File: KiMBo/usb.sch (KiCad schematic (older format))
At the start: 19 parts, among them U10 74LVC2G241, U11 TPD4S012, U2 OSD3358, U8 TPS2051B, U9 TPD4S012

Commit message: Replace most electrolytic cap symbols symbols with the standard, non-polarized (ceramic) cap symbol
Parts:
- C27, C28, C29: symbol CP1 -> C
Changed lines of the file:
@@
 $EndComp
 $Comp
-L CP1 C29
+L C C29
 U 1 1 584F50A3
 P 8150 1650
@@
 $EndComp
 $Comp
-L CP1 C27
+L C C27
 U 1 1 58524285
 P 6250 4600
@@
 $EndComp
 $Comp
-L CP1 C26
-U 1 1 5852A62D
-P 2500 4400
-F 0 "C26" H 2615 4446 50  0000 L CNN
-F 1 "220μF" H 2615 4355 50  0000 L CNN
-F 2 "" H 2500 4400 50  0001 C CNN
-F 3 "" H 2500 4400 50  0000 C CNN
-	1    2500 4400
-	-1   0    0    -1
-$EndComp
-$Comp
 L GND #PWR0115
 U 1 1 5852A6BE
@@
 $EndComp
 $Comp
-L CP1 C28
+L C C28
 U 1 1 5852C2E6
 P 8000 4100
@@
 	6550 2050 6550 1600
 Wire Wire Line
-	6550 1600 7700 1600
+	6550 1600 7600 1600
+Wire Wire Line
+	7600 1600 7700 1600
 Wire Wire Line
 	7600 1600 7600 2250
@@
 	3600 1600 3600 1650
 Wire Wire Line
-	3450 1650 3650 1650
-Wire Wire Line
-	3450 1750 3650 1750
+	3450 1650 3600 1650
+Wire Wire Line
+	3600 1650 3650 1650
+Wire Wire Line
+	3450 1750 3500 1750
+Wire Wire Line
+	3500 1750 3650 1750
 Wire Wire Line
 	3600 1250 3600 1300
@@
 	3500 1300 3500 1250
 Wire Wire Line
-	3500 1250 3600 1250
+	3500 1250 3550 1250
+Wire Wire Line
+	3550 1250 3600 1250
 Wire Wire Line
 	3550 1200 3550 1250
@@
 	5150 4200 6400 4200
 Wire Wire Line
-	4450 4100 5850 4100
+	4450 4100 4500 4100
+Wire Wire Line
+	4500 4100 5750 4100
+Wire Wire Line
+	5750 4100 5850 4100
 Wire Wire Line
 	6100 4800 6250 4800
 Wire Wire Line
-	6250 4750 6250 4850
+	6250 4750 6250 4800
+Wire Wire Line
+	6250 4800 6250 4850
 Connection ~ 6250 4800
 Wire Wire Line
 	6100 4600 6100 4400
 Wire Wire Line
-	5750 4400 6250 4400
+	5750 4400 6100 4400
+Wire Wire Line
+	6100 4400 6250 4400
 Wire Wire Line
 	6250 4400 6250 4450
@@
 	5150 4700 5150 4200
 Wire Wire Line
-	5750 4050 5750 4400
+	5750 4050 5750 4100
+Wire Wire Line
+	5750 4100 5750 4400
 Connection ~ 6100 4400
 Connection ~ 5750 4100
@@
 	4500 4300 4450 4300
 Wire Wire Line
-	4500 4100 4500 4300
+	4500 4100 4500 4200
+Wire Wire Line
+	4500 4200 4500 4300
 Wire Wire Line
 	4450 4200 4500 4200
@@
 	4500 4500 4450 4500
 Wire Wire Line
-	4450 4400 4700 4400
+	4450 4400 4550 4400
+Wire Wire Line
+	4550 4400 4700 4400
 Wire Wire Line
 	5050 4350 5050 4400
@@
 Connection ~ 4550 4400
 Wire Wire Line
-	2500 4200 3550 4200
+	2500 4200 3500 4200
+Wire Wire Line
+	3500 4200 3550 4200
 Wire Wire Line
 	3500 4200 3500 4300
@@
 	3500 4300 3550 4300
 Wire Wire Line
-	2500 4150 2500 4250
+	2500 4150 2500 4200
+Wire Wire Line
+	2500 4200 2500 4250
 Connection ~ 3500 4200
 Wire Wire Line
@@
 	2700 4100 2700 4250
 Wire Wire Line
-	2800 4400 3550 4400
+	2800 4400 3500 4400
+Wire Wire Line
+	3500 4400 3550 4400
 Wire Wire Line
 	3500 4450 3500 4400
@@
 	8150 4300 8000 4300
 Wire Wire Line
-	8000 4250 8000 4350
-Wire Wire Line
-	8150 3850 8150 4100
+	8000 4250 8000 4300
+Wire Wire Line
+	8000 4300 8000 4350
+Wire Wire Line
+	8150 3850 8150 3900
+Wire Wire Line
+	8150 3900 8150 4100
 Wire Wire Line
 	8150 3900 8000 3900
@@
 F 0 "R53" H 5819 3946 50  0000 L CNN
 F 1 "100mΩ" H 5819 3855 50  0000 L CNN
-F 2 "" V 5680 3900 50  0000 C CNN
+F 2 "" V 5680 3900 50  0001 C CNN
 F 3 "" H 5750 3900 50  0000 C CNN
 	1    5750 3900
@@
 Text Notes 5200 3800 0    60   ~ 0
 73L3R10J
+$Comp
+L CP1 C26
+U 1 1 58EB0DF2
+P 2500 4400
+F 0 "C26" H 2615 4446 50  0000 L CNN
+F 1 "220μF" H 2615 4355 50  0000 L CNN
+F 2 "" H 2500 4400 50  0000 C CNN
+F 3 "" H 2500 4400 50  0000 C CNN
+	1    2500 4400
+	-1   0    0    -1
+$EndComp
 $EndSCHEMATC

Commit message: Associate more footprints
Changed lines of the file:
@@
 	6550 2050 6550 1600
 Wire Wire Line
-	6550 1600 7600 1600
-Wire Wire Line
-	7600 1600 7700 1600
+	6550 1600 7700 1600
 Wire Wire Line
 	7600 1600 7600 2250
@@
 	3600 1600 3600 1650
 Wire Wire Line
-	3450 1650 3600 1650
-Wire Wire Line
-	3600 1650 3650 1650
-Wire Wire Line
-	3450 1750 3500 1750
-Wire Wire Line
-	3500 1750 3650 1750
+	3450 1650 3650 1650
+Wire Wire Line
+	3450 1750 3650 1750
 Wire Wire Line
 	3600 1250 3600 1300
@@
 	3500 1300 3500 1250
 Wire Wire Line
-	3500 1250 3550 1250
-Wire Wire Line
-	3550 1250 3600 1250
+	3500 1250 3600 1250
 Wire Wire Line
 	3550 1200 3550 1250
@@
 	5150 4200 6400 4200
 Wire Wire Line
-	4450 4100 4500 4100
-Wire Wire Line
-	4500 4100 5750 4100
-Wire Wire Line
-	5750 4100 5850 4100
+	4450 4100 5850 4100
 Wire Wire Line
 	6100 4800 6250 4800
 Wire Wire Line
-	6250 4750 6250 4800
-Wire Wire Line
-	6250 4800 6250 4850
+	6250 4750 6250 4850
 Connection ~ 6250 4800
 Wire Wire Line
 	6100 4600 6100 4400
 Wire Wire Line
-	5750 4400 6100 4400
-Wire Wire Line
-	6100 4400 6250 4400
+	5750 4400 6250 4400
 Wire Wire Line
 	6250 4400 6250 4450
@@
 	5150 4700 5150 4200
 Wire Wire Line
-	5750 4050 5750 4100
-Wire Wire Line
-	5750 4100 5750 4400
+	5750 4050 5750 4400
 Connection ~ 6100 4400
 Connection ~ 5750 4100
@@
 	4500 4300 4450 4300
 Wire Wire Line
-	4500 4100 4500 4200
-Wire Wire Line
-	4500 4200 4500 4300
+	4500 4100 4500 4300
 Wire Wire Line
 	4450 4200 4500 4200
@@
 	4500 4500 4450 4500
 Wire Wire Line
-	4450 4400 4550 4400
-Wire Wire Line
-	4550 4400 4700 4400
+	4450 4400 4700 4400
 Wire Wire Line
 	5050 4350 5050 4400
@@
 Connection ~ 4550 4400
 Wire Wire Line
-	2500 4200 3500 4200
-Wire Wire Line
-	3500 4200 3550 4200
+	2500 4200 3550 4200
 Wire Wire Line
 	3500 4200 3500 4300
@@
 	3500 4300 3550 4300
 Wire Wire Line
-	2500 4150 2500 4200
-Wire Wire Line
-	2500 4200 2500 4250
+	2500 4150 2500 4250
 Connection ~ 3500 4200
 Wire Wire Line
@@
 	2700 4100 2700 4250
 Wire Wire Line
-	2800 4400 3500 4400
-Wire Wire Line
-	3500 4400 3550 4400
+	2800 4400 3550 4400
 Wire Wire Line
 	3500 4450 3500 4400
@@
 	8150 4300 8000 4300
 Wire Wire Line
-	8000 4250 8000 4300
-Wire Wire Line
-	8000 4300 8000 4350
-Wire Wire Line
-	8150 3850 8150 3900
-Wire Wire Line
-	8150 3900 8150 4100
+	8000 4250 8000 4350
+Wire Wire Line
+	8150 3850 8150 4100
 Wire Wire Line
 	8150 3900 8000 3900
@@
 F 0 "C26" H 2615 4446 50  0000 L CNN
 F 1 "220μF" H 2615 4355 50  0000 L CNN
-F 2 "" H 2500 4400 50  0000 C CNN
+F 2 "" H 2500 4400 50  0001 C CNN
 F 3 "" H 2500 4400 50  0000 C CNN
 	1    2500 4400

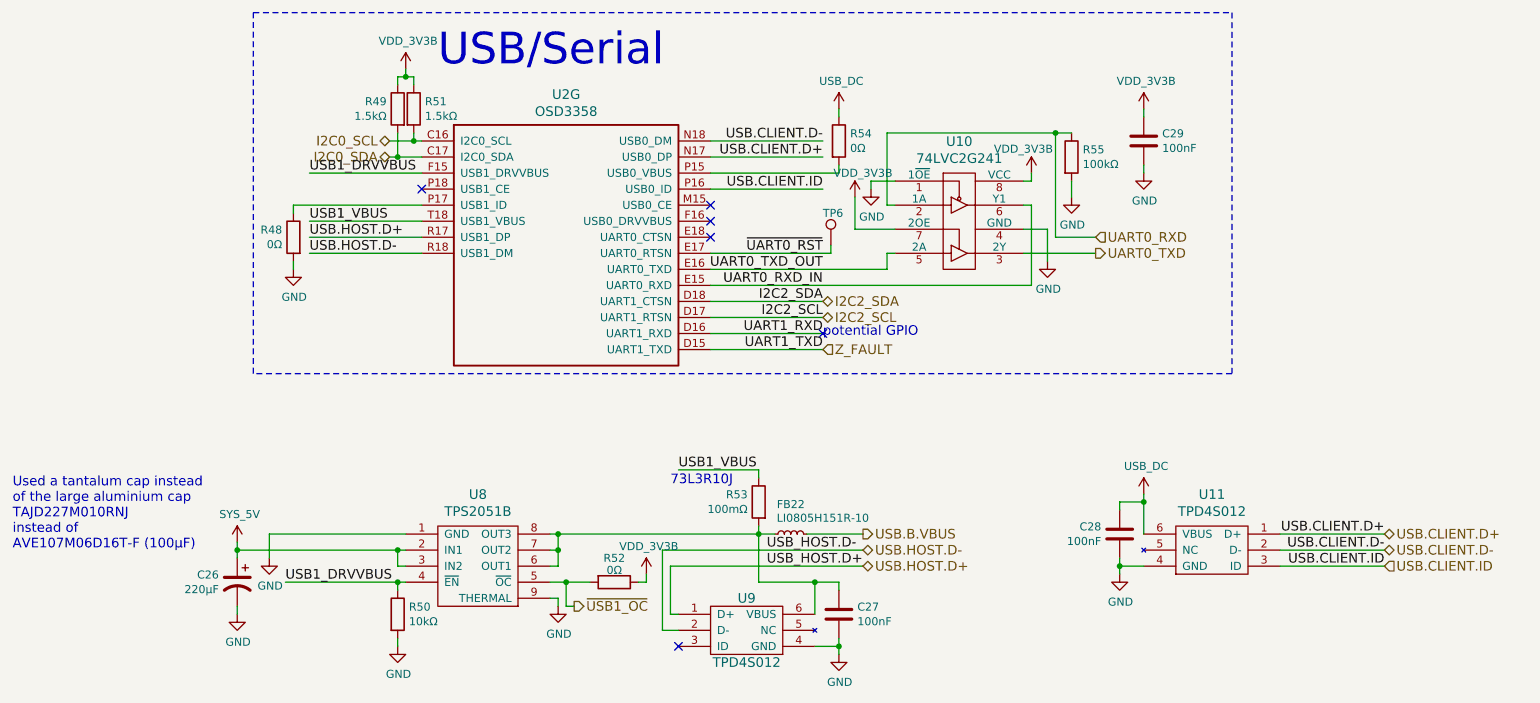
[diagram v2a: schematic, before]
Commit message: Add equivalent annotations document, associate more footprints
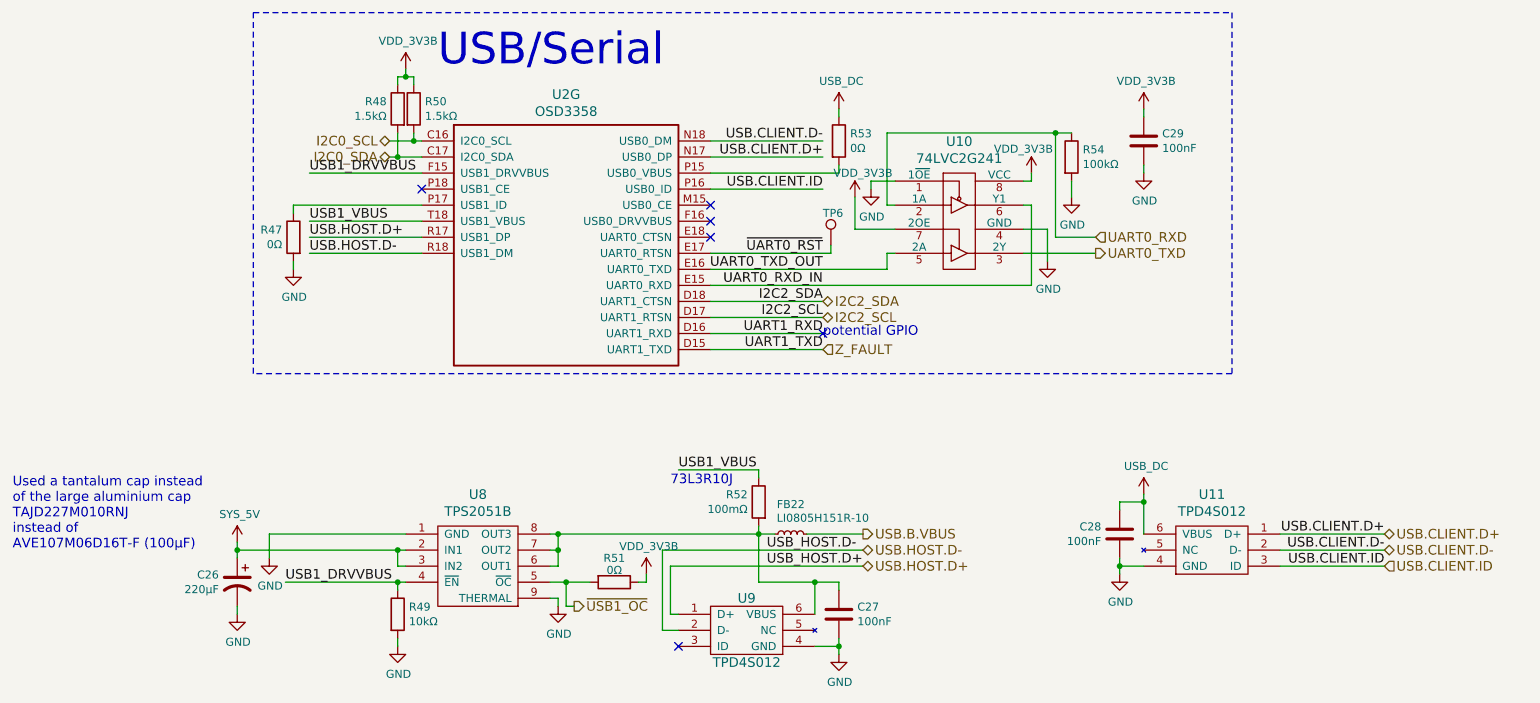
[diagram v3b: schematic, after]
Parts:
- C27, C28, C29: footprint (none) -> Capacitors_SMD:C_0402
- R47: renamed from R48; footprint (none) -> Resistors_SMD:R_0402
- R48: renamed from R49; footprint (none) -> Resistors_SMD:R_0402
- R49: renamed from R50; footprint (none) -> Resistors_SMD:R_0402
- R50: renamed from R51; footprint (none) -> Resistors_SMD:R_0402
- R51: renamed from R52; footprint (none) -> Resistors_SMD:R_0402
- R52: renamed from R53; footprint (none) -> Resistors_SMD:R_0402
- R53: renamed from R54; footprint (none) -> Resistors_SMD:R_0402
- R54: renamed from R55; footprint (none) -> Resistors_SMD:R_0402
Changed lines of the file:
@@
 $EndComp
 $Comp
-L GND #PWR0108
+L GND #PWR0107
 U 1 1 584F5078
 P 7550 2400
-F 0 "#PWR0108" H 7550 2150 50  0001 C CNN
+F 0 "#PWR0107" H 7550 2150 50  0001 C CNN
 F 1 "GND" H 7555 2227 50  0000 C CNN
 F 2 "" H 7550 2400 50  0000 C CNN
@@
 UART0_RXD_IN
 $Comp
-L R R55
+L R R54
 U 1 1 584F5085
 P 7700 1750
-F 0 "R55" H 7770 1796 50  0000 L CNN
+F 0 "R54" H 7770 1796 50  0000 L CNN
 F 1 "100kΩ" H 7770 1705 50  0000 L CNN
-F 2 "" V 7630 1750 50  0001 C CNN
+F 2 "Resistors_SMD:R_0402" V 7630 1750 50  0001 C CNN
 F 3 "" H 7700 1750 50  0000 C CNN
 	1    7700 1750
@@
 $EndComp
 $Comp
-L GND #PWR0109
+L GND #PWR0108
 U 1 1 584F508C
 P 6450 1950
-F 0 "#PWR0109" H 6450 1700 50  0001 C CNN
+F 0 "#PWR0108" H 6450 1700 50  0001 C CNN
 F 1 "GND" H 6455 1777 50  0000 C CNN
 F 2 "" H 6450 1950 50  0000 C CNN
@@
 UART0_TXD_OUT
 $Comp
-L GND #PWR0110
+L GND #PWR0109
 U 1 1 584F509A
 P 7700 2000
-F 0 "#PWR0110" H 7700 1750 50  0001 C CNN
+F 0 "#PWR0109" H 7700 1750 50  0001 C CNN
 F 1 "GND" H 7705 1827 50  0000 C CNN
 F 2 "" H 7700 2000 50  0000 C CNN
@@
 F 0 "C29" H 8265 1696 50  0000 L CNN
 F 1 "100nF" H 8265 1605 50  0000 L CNN
-F 2 "" H 8150 1650 50  0001 C CNN
+F 2 "Capacitors_SMD:C_0402" H 8150 1650 50  0001 C CNN
 F 3 "" H 8150 1650 50  0000 C CNN
 	1    8150 1650
@@
 $EndComp
 $Comp
-L GND #PWR0111
+L GND #PWR0110
 U 1 1 584F50AA
 P 8150 1850
-F 0 "#PWR0111" H 8150 1600 50  0001 C CNN
+F 0 "#PWR0110" H 8150 1600 50  0001 C CNN
 F 1 "GND" H 8155 1677 50  0000 C CNN
 F 2 "" H 8150 1850 50  0000 C CNN
@@
 NoConn ~ 5450 2150
 $Comp
-L R R54
+L R R53
 U 1 1 584F50C1
 P 6250 1650
-F 0 "R54" H 6320 1696 50  0000 L CNN
+F 0 "R53" H 6320 1696 50  0000 L CNN
 F 1 "0Ω" H 6320 1605 50  0000 L CNN
-F 2 "" V 6180 1650 50  0001 C CNN
+F 2 "Resistors_SMD:R_0402" V 6180 1650 50  0001 C CNN
 F 3 "" H 6250 1650 50  0000 C CNN
 	1    6250 1650
@@
 NoConn ~ 3650 1950
 $Comp
-L R R48
+L R R47
 U 1 1 584F50D1
 P 2850 2250
-F 0 "R48" H 2920 2296 50  0000 L CNN
+F 0 "R47" H 2920 2296 50  0000 L CNN
 F 1 "0Ω" H 2920 2205 50  0000 L CNN
-F 2 "" V 2780 2250 50  0001 C CNN
+F 2 "Resistors_SMD:R_0402" V 2780 2250 50  0001 C CNN
 F 3 "" H 2850 2250 50  0000 C CNN
 	1    2850 2250
@@
 $EndComp
 $Comp
-L GND #PWR0112
+L GND #PWR0111
 U 1 1 584F50D8
 P 2850 2450
-F 0 "#PWR0112" H 2850 2200 50  0001 C CNN
+F 0 "#PWR0111" H 2850 2200 50  0001 C CNN
 F 1 "GND" H 2855 2277 50  0000 C CNN
 F 2 "" H 2850 2450 50  0000 C CNN
@@
 USB1_DRVVBUS
 $Comp
-L R R49
+L R R48
 U 1 1 584F50E0
 P 3500 1450
-F 0 "R49" H 3569 1496 50  0000 L CNN
+F 0 "R48" H 3569 1496 50  0000 L CNN
 F 1 "1.5kΩ" H 3569 1405 50  0000 L CNN
-F 2 "" V 3430 1450 50  0001 C CNN
+F 2 "Resistors_SMD:R_0402" V 3430 1450 50  0001 C CNN
 F 3 "" H 3500 1450 50  0000 C CNN
 	1    3500 1450
@@
 $EndComp
 $Comp
-L R R51
+L R R50
 U 1 1 584F50E7
 P 3600 1450
-F 0 "R51" H 3670 1496 50  0000 L CNN
+F 0 "R50" H 3670 1496 50  0000 L CNN
 F 1 "1.5kΩ" H 3670 1405 50  0000 L CNN
-F 2 "" V 3530 1450 50  0001 C CNN
+F 2 "Resistors_SMD:R_0402" V 3530 1450 50  0001 C CNN
 F 3 "" H 3600 1450 50  0000 C CNN
 	1    3600 1450
@@
 F 0 "C27" H 6365 4646 50  0000 L CNN
 F 1 "100nF" H 6365 4555 50  0000 L CNN
-F 2 "" H 6250 4600 50  0001 C CNN
+F 2 "Capacitors_SMD:C_0402" H 6250 4600 50  0001 C CNN
 F 3 "" H 6250 4600 50  0000 C CNN
 	1    6250 4600
@@
 $EndComp
 $Comp
-L GND #PWR0113
+L GND #PWR0112
 U 1 1 585243B8
 P 6250 4850
-F 0 "#PWR0113" H 6250 4600 50  0001 C CNN
+F 0 "#PWR0112" H 6250 4600 50  0001 C CNN
 F 1 "GND" H 6255 4677 50  0000 C CNN
 F 2 "" H 6250 4850 50  0000 C CNN
@@
 $EndComp
 $Comp
-L GND #PWR0114
+L GND #PWR0113
 U 1 1 58528602
 P 4500 4550
-F 0 "#PWR0114" H 4500 4300 50  0001 C CNN
+F 0 "#PWR0113" H 4500 4300 50  0001 C CNN
 F 1 "GND" H 4505 4377 50  0000 C CNN
 F 2 "" H 4500 4550 50  0000 C CNN
@@
 $EndComp
 $Comp
-L R R52
+L R R51
 U 1 1 58528C30
 P 4850 4400
-F 0 "R52" V 4700 4400 50  0000 C CNN
+F 0 "R51" V 4700 4400 50  0000 C CNN
 F 1 "0Ω" V 4775 4400 50  0000 C CNN
-F 2 "" V 4780 4400 50  0001 C CNN
+F 2 "Resistors_SMD:R_0402" V 4780 4400 50  0001 C CNN
 F 3 "" H 4850 4400 50  0000 C CNN
 	1    4850 4400
@@
 $EndComp
 $Comp
-L GND #PWR0115
+L GND #PWR0114
 U 1 1 5852A6BE
 P 2500 4600
-F 0 "#PWR0115" H 2500 4350 50  0001 C CNN
+F 0 "#PWR0114" H 2500 4350 50  0001 C CNN
 F 1 "GND" H 2505 4427 50  0000 C CNN
 F 2 "" H 2500 4600 50  0000 C CNN
@@
 $EndComp
 $Comp
-L GND #PWR0116
+L GND #PWR0115
 U 1 1 5852A82F
 P 2700 4250
-F 0 "#PWR0116" H 2700 4000 50  0001 C CNN
+F 0 "#PWR0115" H 2700 4000 50  0001 C CNN
 F 1 "GND" H 2705 4077 50  0000 C CNN
 F 2 "" H 2700 4250 50  0000 C CNN
@@
 USB1_DRVVBUS
 $Comp
-L R R50
+L R R49
 U 1 1 5852B51B
 P 3500 4600
-F 0 "R50" H 3570 4646 50  0000 L CNN
+F 0 "R49" H 3570 4646 50  0000 L CNN
 F 1 "10kΩ" H 3570 4555 50  0000 L CNN
-F 2 "" V 3430 4600 50  0001 C CNN
+F 2 "Resistors_SMD:R_0402" V 3430 4600 50  0001 C CNN
 F 3 "" H 3500 4600 50  0000 C CNN
 	1    3500 4600
@@
 $EndComp
 $Comp
-L GND #PWR0117
+L GND #PWR0116
 U 1 1 5852B68C
 P 3500 4800
-F 0 "#PWR0117" H 3500 4550 50  0001 C CNN
+F 0 "#PWR0116" H 3500 4550 50  0001 C CNN
 F 1 "GND" H 3505 4627 50  0000 C CNN
 F 2 "" H 3500 4800 50  0000 C CNN
@@
 F 0 "C28" H 8115 4146 50  0000 L CNN
 F 1 "100nF" H 8115 4055 50  0000 L CNN
-F 2 "" H 8000 4100 50  0001 C CNN
+F 2 "Capacitors_SMD:C_0402" H 8000 4100 50  0001 C CNN
 F 3 "" H 8000 4100 50  0000 C CNN
 	1    8000 4100
@@
 I2C2_SDA
 $Comp
-L USB_DC #PWR0118
+L USB_DC #PWR0117
 U 1 1 59F94F9A
 P 8150 3850
-F 0 "#PWR0118" H 8150 3700 50  0001 C CNN
+F 0 "#PWR0117" H 8150 3700 50  0001 C CNN
 F 1 "USB_DC" H 8165 4023 50  0000 C CNN
 F 2 "" H 8150 3850 50  0000 C CNN
@@
 $EndComp
 $Comp
-L SYS_5V #PWR0119
+L SYS_5V #PWR0118
 U 1 1 59F970D0
 P 2500 4150
-F 0 "#PWR0119" H 2500 4000 50  0001 C CNN
+F 0 "#PWR0118" H 2500 4000 50  0001 C CNN
 F 1 "SYS_5V" H 2515 4323 50  0000 C CNN
 F 2 "" H 2500 4150 50  0000 C CNN
@@
 $EndComp
 $Comp
-L VDD_3V3B #PWR0120
+L VDD_3V3B #PWR0119
 U 1 1 59FBF8B1
 P 6350 2000
-F 0 "#PWR0120" H 6350 1850 50  0001 C CNN
+F 0 "#PWR0119" H 6350 1850 50  0001 C CNN
 F 1 "VDD_3V3B" H 6400 2150 50  0000 C CNN
 F 2 "" H 6350 2000 50  0000 C CNN
@@
 $EndComp
 $Comp
-L VDD_3V3B #PWR0121
+L VDD_3V3B #PWR0120
 U 1 1 59FBF8FC
 P 7450 1850
-F 0 "#PWR0121" H 7450 1700 50  0001 C CNN
+F 0 "#PWR0120" H 7450 1700 50  0001 C CNN
 F 1 "VDD_3V3B" H 7400 2000 50  0000 C CNN
 F 2 "" H 7450 1850 50  0000 C CNN
@@
 $EndComp
 $Comp
-L VDD_3V3B #PWR0122
+L VDD_3V3B #PWR0121
 U 1 1 59FC0162
 P 8150 1450
-F 0 "#PWR0122" H 8150 1300 50  0001 C CNN
+F 0 "#PWR0121" H 8150 1300 50  0001 C CNN
 F 1 "VDD_3V3B" H 8165 1623 50  0000 C CNN
 F 2 "" H 8150 1450 50  0000 C CNN
@@
 $EndComp
 $Comp
-L USB_DC #PWR0123
+L USB_DC #PWR0122
 U 1 1 59FEDDB0
 P 6250 1450
-F 0 "#PWR0123" H 6250 1300 50  0001 C CNN
+F 0 "#PWR0122" H 6250 1300 50  0001 C CNN
 F 1 "USB_DC" H 6265 1623 50  0000 C CNN
 F 2 "" H 6250 1450 50  0000 C CNN
@@
 $EndComp
 $Comp
-L VDD_3V3B #PWR0124
+L VDD_3V3B #PWR0123
 U 1 1 5A01DA26
 P 3550 1200
-F 0 "#PWR0124" H 3550 1050 50  0001 C CNN
+F 0 "#PWR0123" H 3550 1050 50  0001 C CNN
 F 1 "VDD_3V3B" H 3565 1373 50  0000 C CNN
 F 2 "" H 3550 1200 50  0000 C CNN
@@
 potential GPIO
 $Comp
-L VDD_3V3B #PWR0125
+L VDD_3V3B #PWR0124
 U 1 1 5AF563FC
 P 5050 4350
-F 0 "#PWR0125" H 5050 4200 50  0001 C CNN
+F 0 "#PWR0124" H 5050 4200 50  0001 C CNN
 F 1 "VDD_3V3B" H 5065 4523 50  0000 C CNN
 F 2 "" H 5050 4350 50  0000 C CNN
@@
 $EndComp
 $Comp
-L GND #PWR0126
+L GND #PWR0125
 U 1 1 5BC77EEA
 P 8000 4350
-F 0 "#PWR0126" H 8000 4100 50  0001 C CNN
+F 0 "#PWR0125" H 8000 4100 50  0001 C CNN
 F 1 "GND" H 8005 4177 50  0000 C CNN
 F 2 "" H 8000 4350 50  0000 C CNN
@@
 	6200 2350 6200 2300
 $Comp
-L R R53
+L R R52
 U 1 1 58DC7D9A
 P 5750 3900
-F 0 "R53" H 5819 3946 50  0000 L CNN
+F 0 "R52" H 5819 3946 50  0000 L CNN
 F 1 "100mΩ" H 5819 3855 50  0000 L CNN
-F 2 "" V 5680 3900 50  0001 C CNN
+F 2 "Resistors_SMD:R_0402" V 5680 3900 50  0001 C CNN
 F 3 "" H 5750 3900 50  0000 C CNN
 	1    5750 3900

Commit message: Leave SPI0 free for a display, reassign pins so SPI1 is available
Fix some typos/errors
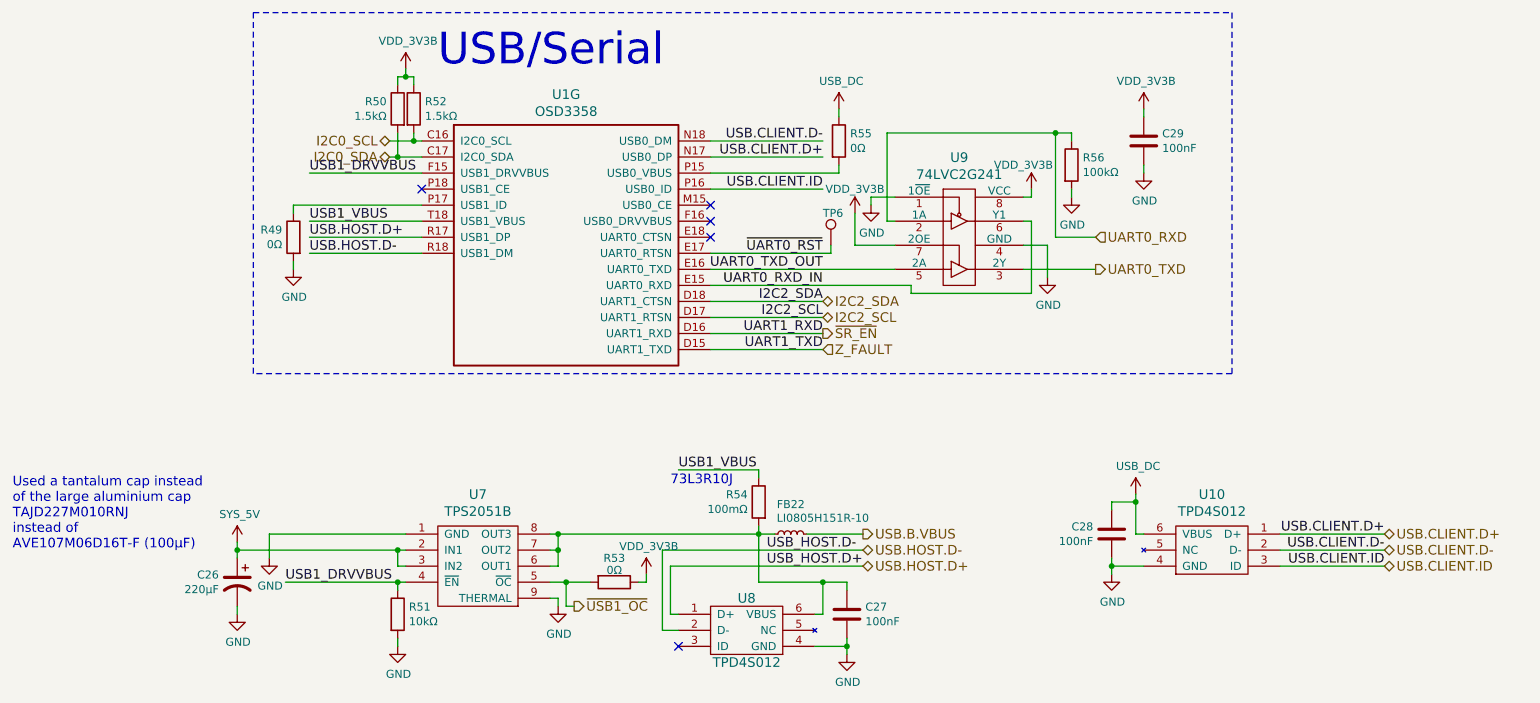
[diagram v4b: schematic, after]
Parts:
- renumbered R47 to R49, R48 to R50, R49 to R51, R50 to R52, R51 to R53, R52 to R54, R53 to R55, R54 to R56, U2 to U1, U11 to U10, U8 to U7, U9 to U8, U10 to U9
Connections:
- net UART1_RXD renamed ~SR_EN
- no-connect marks 6 -> 5
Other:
- note removed: "potential GPIO"
- moved on the sheet: C27, C28, R56, U9
